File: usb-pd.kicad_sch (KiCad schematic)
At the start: 49 parts, among them J11 12401598E4_2A, U23 STUSB4500QTR

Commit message: Introduce component standardization
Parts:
- C152: footprint sa800u-baseboard-hw-footprints:0603-cap -> sa800u-baseboard-hw-footprints:C_0603_1608Metric; Author (none) -> Antmicro; License (none) -> Apache-2.0
- C153: footprint sa800u-baseboard-hw-footprints:0603-cap -> sa800u-baseboard-hw-footprints:C_0603_1608Metric; Author (none) -> Antmicro; License (none) -> Apache-2.0; Manufacturer WALSIN -> Walsin
- C154, C156, C157: footprint sa800u-baseboard-hw-footprints:0402-cap -> sa800u-baseboard-hw-footprints:C_0402_1005Metric; Author (none) -> Antmicro; License (none) -> Apache-2.0
- C155: footprint sa800u-baseboard-hw-footprints:0402-cap -> sa800u-baseboard-hw-footprints:C_0402_1005Metric; Author (none) -> Antmicro; Dielectric (none) -> X5R; License (none) -> Apache-2.0; Voltage (none) -> 50V
- D33, D34, D37: footprint sa800u-baseboard-hw-footprints:RESC0603X26N -> sa800u-baseboard-hw-footprints:D_0201_0603Metric; Author (none) -> Antmicro; License (none) -> Apache-2.0; Manufacturer nexperia -> Nexperia
- D35: footprint sa800u-baseboard-hw-footprints:SOD-323F -> sa800u-baseboard-hw-footprints:D_SOD-323F; Author (none) -> Antmicro; License (none) -> Apache-2.0; Manufacturer NEXPERIA -> Nexperia
- D36: Author (none) -> Antmicro; License (none) -> Apache-2.0
- J11: footprint sa800u-baseboard-hw-footprints:USB-C_Female_12401X -> sa800u-baseboard-hw-footprints:USB-C_12401610E4_2A; Author (none) -> Antmicro; License (none) -> Apache-2.0; Manufacturer Amphenol ICC (Commercial Products) -> Amphenol
- Q17: renamed from Q?; value (none) -> SQS401EN-T1_BE3; footprint (none) -> sa800u-baseboard-hw-footprints:Vishay_PowerPAK_1212-8_Single; Author (none) -> Antmicro; License (none) -> Apache-2.0
- R153: renamed from R?; value (none) -> R_10k_0402; footprint (none) -> sa800u-baseboard-hw-footprints:R_0402_1005Metric; Author (none) -> Antmicro; License (none) -> Apache-2.0; MPN CRCW040210K0FKEDHP -> CR0402-FX-1002GLF; Manufacturer VISHAY -> Bourns; Tolerance (none) -> 1%
- R154, R155, R156, R157, R160: footprint sa800u-baseboard-hw-footprints:0402-res -> sa800u-baseboard-hw-footprints:R_0402_1005Metric; Author (none) -> Antmicro; License (none) -> Apache-2.0; MPN CRCW0402100KFKEDHP -> CR0402-FX-1003GLF; Manufacturer VISHAY -> Bourns; Tolerance (none) -> 1%
- R158: footprint sa800u-baseboard-hw-footprints:0402-res -> sa800u-baseboard-hw-footprints:R_0402_1005Metric; Author (none) -> Antmicro; License (none) -> Apache-2.0; MPN CRCW0402470RFKED -> CR0402-FX-4700GLF; Manufacturer VISHAY -> Bourns; Tolerance (none) -> 1%
- R159, R166: footprint sa800u-baseboard-hw-footprints:0402-res -> sa800u-baseboard-hw-footprints:R_0402_1005Metric; Author (none) -> Antmicro; License (none) -> Apache-2.0; Manufacturer BOURNS -> Bourns; Tolerance (none) -> 1%
- R161: footprint sa800u-baseboard-hw-footprints:0402-res -> sa800u-baseboard-hw-footprints:R_0402_1005Metric; Author (none) -> Antmicro; License (none) -> Apache-2.0; MPN ERJ-2RKF2202X -> CR0402-FX-2202GLF; Manufacturer Panasonic -> Bourns; Tolerance (none) -> 1%
- R162, R163, R164, R165: renamed from R?; value (none) -> R_0R_0402; footprint (none) -> sa800u-baseboard-hw-footprints:R_0402_1005Metric; Author (none) -> Antmicro; Current (none) -> 1A; License (none) -> Apache-2.0; Manufacturer PANASONIC -> Panasonic
- R167, R168, R170, R172: footprint sa800u-baseboard-hw-footprints:0402-res -> sa800u-baseboard-hw-footprints:R_0402_1005Metric; Author (none) -> Antmicro; License (none) -> Apache-2.0; MPN MCS04020C4701FE000 -> CR0402-FX-4701GLF; Manufacturer VISHAY -> Bourns; Tolerance (none) -> 1%
- R169: footprint sa800u-baseboard-hw-footprints:0402-res -> sa800u-baseboard-hw-footprints:R_0402_1005Metric; Author (none) -> Antmicro; License (none) -> Apache-2.0; MPN ERJ2RKF1101X -> CR0402-FX-1101GLF; Manufacturer PANASONIC_ELECTRONIC_COMPONENTS -> Bourns; Tolerance (none) -> 1%
- R171: footprint sa800u-baseboard-hw-footprints:0402-res -> sa800u-baseboard-hw-footprints:R_0402_1005Metric; Author (none) -> Antmicro; License (none) -> Apache-2.0; MPN RC0402JR-07510RL -> CR0402-FX-5100GLF; Manufacturer Yageo -> Bourns; Tolerance (none) -> 1%
- R173: footprint sa800u-baseboard-hw-footprints:0402-res -> sa800u-baseboard-hw-footprints:R_0402_1005Metric; Author (none) -> Antmicro; License (none) -> Apache-2.0; MPN RC0402FR-07750RL -> CR0402-FX-7500GLF; Manufacturer Yageo -> Bourns; Tolerance (none) -> 1%
- R174: footprint sa800u-baseboard-hw-footprints:0402-res -> sa800u-baseboard-hw-footprints:R_0402_1005Metric; Author (none) -> Antmicro; License (none) -> Apache-2.0; MPN RK73H1ETTP2701F -> CR0402-FX-2701GLF; Manufacturer KOA -> Bourns; Tolerance (none) -> 1%
- TP86, TP87, TP88, TP89, TP90, TP91, TP92, TP93, TP94, TP95, TP96, TP97: renamed from TP?; value (none) -> TP_0.75mm_SMD; footprint (none) -> sa800u-baseboard-hw-footprints:TP_SMD_0.75mm; symbol sa800u-baseboard-hw:TP_SMD_0_75MM -> sa800u-baseboard-hw:TP_0.75mm_SMD; Author (none) -> Antmicro; License (none) -> Apache-2.0
- TP98: renamed from TP?; value (none) -> TP_0.75mm_SMD; footprint (none) -> sa800u-baseboard-hw-footprints:TP_SMD_0.75mm; symbol sa800u-baseboard-hw:TP -> sa800u-baseboard-hw:TP_0.75mm_SMD; Author (none) -> Antmicro; License (none) -> Apache-2.0
- U23: value STUSB4500QTR -> STUSB4500_QFN; footprint sa800u-baseboard-hw-footprints:QFN50P400X400X90-25N -> sa800u-baseboard-hw-footprints:QFN-24-1EP_4x4mm_EP2.1x2.1mm; symbol sa800u-baseboard-hw:STUSB4500QTR -> sa800u-baseboard-hw:STUSB4500_QFN; Author (none) -> Antmicro; License (none) -> Apache-2.0
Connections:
- net GND: now also C156.2, D36.3; no longer C156.1, D36.2
- net STUSB4500_PWR_OK3: now also D36.2; no longer D36.3
- net VREG_1V2: now also C156.1; no longer C156.2
- net EN_SINK: now reaches R161.2, U23.16 (VBUS_EN_SNK)
- net VS_DISCH: now reaches R159.2, U23.18 (VBUS_VS_DISCH)
- net DISCH: now reaches R169.2, U23.9 (DISCH)
- net at D36.4: now also R174.2; no longer R173.2
- net at D36.5: now also R173.2; no longer R174.2
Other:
- moved on the sheet: C152, C153, C154, C155, C156, C157, D33, D34, D36, D37, R153, R154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

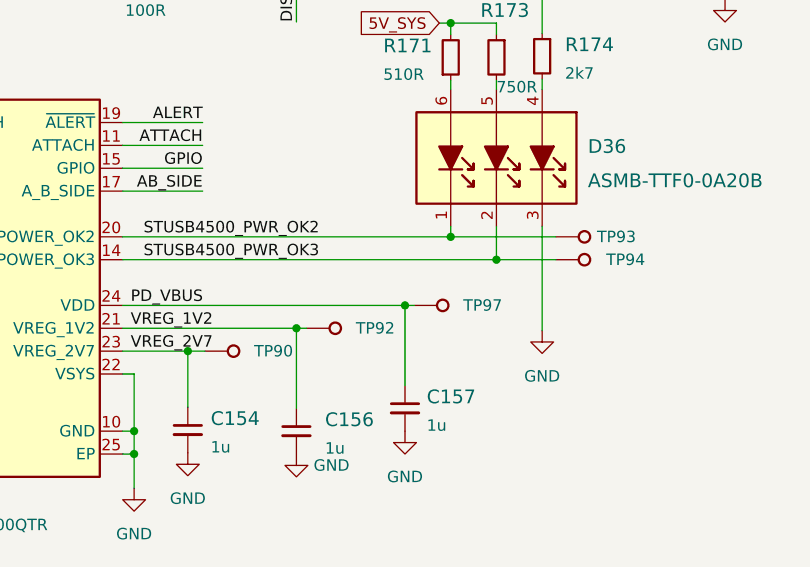
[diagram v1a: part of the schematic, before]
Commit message: Add OHP assets
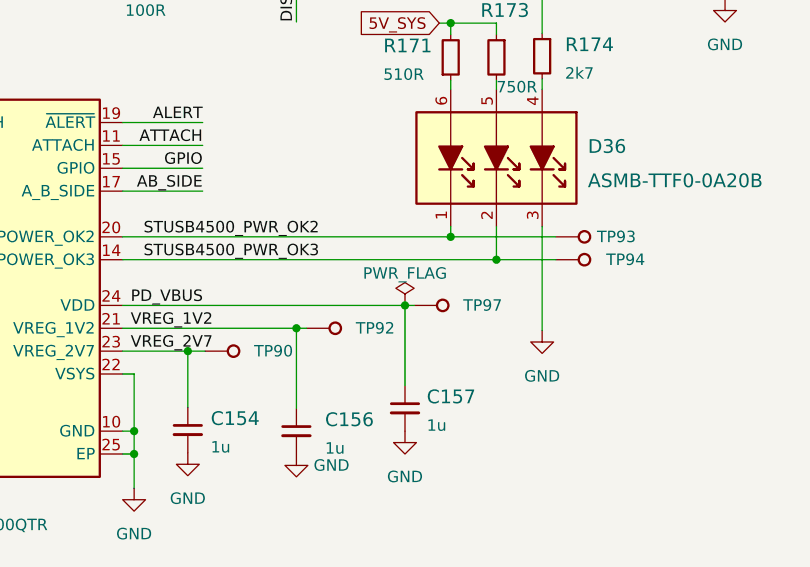
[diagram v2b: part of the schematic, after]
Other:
- company: (none) -> Antmicro Ltd.
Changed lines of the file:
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@@
   (title_block
     (title "SA800U (Snapdragon 845) Baseboard")
-    (date "2023-07-27")
-    (rev "1.0.2")
+    (date "2023-10-19")
+    (rev "1.0.3")
+    (company "Antmicro Ltd.")
     (comment 1 "www.antmicro.com")
-    (comment 2 "Antmicro Ltd.")
   )
   (junction (at 203.581 183.896) (diameter 0) (color 0 0 0 0)
@@
     )
     (pin "1")
+  )
+  (symbol (lib_id "sa800u-baseboard-hw:PWR_FLAG") (at 271.78 181.356 0) (unit 1)
+    (in_bom yes) (on_board yes)
+    (property "Reference" "#FLG0106" (id 0) (at 271.78 179.451 0)
+      (effects (font (size 1.27 1.27)) hide)
+    )
+    (property "Value" "PWR_FLAG" (id 1) (at 271.78 177.8 0))
+    (property "Footprint" "" (id 2) (at 271.78 181.356 0)
+      (effects (font (size 1.27 1.27)) hide)
+    )
+    (property "Datasheet" "~" (id 3) (at 271.78 181.356 0)
+      (effects (font (size 1.27 1.27)) hide)
+    )
+    (pin "1")
